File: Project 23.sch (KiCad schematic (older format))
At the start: 48 parts, among them J11 SRX 1, J12 SRX 2, J13 SWD, J21 Batt, J61 USB_Micro, Q51 Si2315, SW11 UI_Btn, SW12 SW_SPST, U1 STM32F103C(8-B)Tx, U2 MCP73811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

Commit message: Version 0.5
Removed 32k osc and added monting holes.
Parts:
- removed C13, C14: 20p, Capacitors_SMD:C_0805_HandSoldering, symbol Device:C
- removed Y12: 32khz, Project 23:ABS25, symbol Device:Crystal
- added M1, M2: Hole_M2, MountingHole:MountingHole_2.2mm_M2, symbol Connector_Generic:Conn_01x01
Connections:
- wire segments 287 -> 276
- no-connect marks 19 -> 23
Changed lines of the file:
@@
 $EndDescr
-$Comp
-L stm32:STM32F103C(8-B)Tx U1
-U 1 1 5B01BC59
-P 4550 2850
-F 0 "U1" H 4550 2950 50  0000 C CNN
-F 1 "STM32F103C(8-B)Tx" H 4550 2750 50  0000 C CNN
-F 2 "Housings_QFP:LQFP-48_7x7mm_Pitch0.5mm" H 4550 2650 50  0001 C CIN
-F 3 "" H 4550 2850 50  0000 C CNN
-	1    4550 2850
-	1    0    0    -1
-$EndComp
 $Comp
 L power:GND #PWR01
@@
 	1    0    0    -1
 $EndComp
-$Comp
-L Device:Crystal Y12
-U 1 1 5B055736
-P 900 2750
-F 0 "Y12" H 900 2900 50  0000 C CNN
-F 1 "32khz" H 900 2600 50  0000 C CNN
-F 2 "Project 23:ABS25" H 900 2750 50  0001 C CNN
-F 3 "" H 900 2750 50  0001 C CNN
-	1    900  2750
-	1    0    0    -1
-$EndComp
-$Comp
-L Device:C C14
-U 1 1 5B0560D6
-P 1050 3100
-F 0 "C14" H 1075 3200 50  0000 L CNN
-F 1 "20p" H 1075 3000 50  0000 L CNN
-F 2 "Capacitors_SMD:C_0805_HandSoldering" H 1088 2950 50  0001 C CNN
-F 3 "" H 1050 3100 50  0001 C CNN
-	1    1050 3100
-	1    0    0    -1
-$EndComp
-$Comp
-L Device:C C13
-U 1 1 5B0561ED
-P 750 3100
-F 0 "C13" H 775 3200 50  0000 L CNN
-F 1 "20p" H 775 3000 50  0000 L CNN
-F 2 "Capacitors_SMD:C_0805_HandSoldering" H 788 2950 50  0001 C CNN
-F 3 "" H 750 3100 50  0001 C CNN
-	1    750  3100
-	1    0    0    -1
-$EndComp
-$Comp
-L power:GND #PWR023
-U 1 1 5B05692F
-P 900 3400
-F 0 "#PWR023" H 900 3150 50  0001 C CNN
-F 1 "GND" H 900 3250 50  0000 C CNN
-F 2 "" H 900 3400 50  0001 C CNN
-F 3 "" H 900 3400 50  0001 C CNN
-	1    900  3400
-	1    0    0    -1
-$EndComp
 Text Label 8100 750  0    60   ~ 0
 Boost_En
@@
 Connection ~ 6050 6650
 Wire Wire Line
-	1050 2650 1150 2650
-Wire Wire Line
-	1050 2650 1050 2750
-Wire Wire Line
-	750  2550 750  2750
-Wire Wire Line
-	750  2550 1150 2550
-Connection ~ 750  2750
-Connection ~ 1050 2750
-Wire Wire Line
-	750  3250 750  3300
-Wire Wire Line
-	750  3300 900  3300
-Wire Wire Line
-	1050 3300 1050 3250
-Wire Wire Line
-	900  3400 900  3300
-Connection ~ 900  3300
-Wire Wire Line
 	9600 4250 10200 4250
 Wire Wire Line
@@
 	6050 6650 6050 6900
 Wire Wire Line
-	750  2750 750  2950
-Wire Wire Line
-	1050 2750 1050 2950
-Wire Wire Line
-	900  3300 1050 3300
-Wire Wire Line
 	10850 6200 10950 6200
 Wire Wire Line
@@
 Wire Wire Line
 	6300 5900 6600 5900
+$Comp
+L stm32:STM32F103C(8-B)Tx U1
+U 1 1 5B01BC59
+P 4550 2850
+F 0 "U1" H 4550 2950 50  0000 C CNN
+F 1 "STM32F103C(8-B)Tx" H 4550 2750 50  0000 C CNN
+F 2 "Housings_QFP:LQFP-48_7x7mm_Pitch0.5mm" H 4550 2650 50  0001 C CIN
+F 3 "" H 4550 2850 50  0000 C CNN
+	1    4550 2850
+	1    0    0    -1
+$EndComp
+NoConn ~ 1150 2550
+NoConn ~ 1150 2650
+$Comp
+L Connector_Generic:Conn_01x01 M1
+U 1 1 5BBF4E00
+P 6600 6350
+F 0 "M1" H 6679 6392 50  0000 L CNN
+F 1 "Hole_M2" H 6679 6301 50  0000 L CNN
+F 2 "MountingHole:MountingHole_2.2mm_M2" H 6600 6350 50  0001 C CNN
+F 3 "~" H 6600 6350 50  0001 C CNN
+	1    6600 6350
+	1    0    0    -1
+$EndComp
+$Comp
+L Connector_Generic:Conn_01x01 M2
+U 1 1 5BBF5814
+P 6600 6550
+F 0 "M2" H 6679 6592 50  0000 L CNN
+F 1 "Hole_M2" H 6679 6501 50  0000 L CNN
+F 2 "MountingHole:MountingHole_2.2mm_M2" H 6600 6550 50  0001 C CNN
+F 3 "~" H 6600 6550 50  0001 C CNN
+	1    6600 6550
+	1    0    0    -1
+$EndComp
+NoConn ~ 6400 6350
+NoConn ~ 6400 6550
 $EndSCHEMATC

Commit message: Reorganized sch
Move Sch over to a larger page, added physical drawing of borad.
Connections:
- wire segments 276 -> 273
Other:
- note added: "3V3 PSU\n"
- note added: "5V PSU\n"
- note added: "BATT CHR"
- note added: "ICSP\n\n"
- note added: "LED"
- note added: "OLED"
- note added: "SEN CON\n"
- note added: "UI BUTTONS\n"
- note added: "USB"
- moved on the sheet: C11, C12, C16, C17, C18, C19, C21, C22, C31, C32, C41, C42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

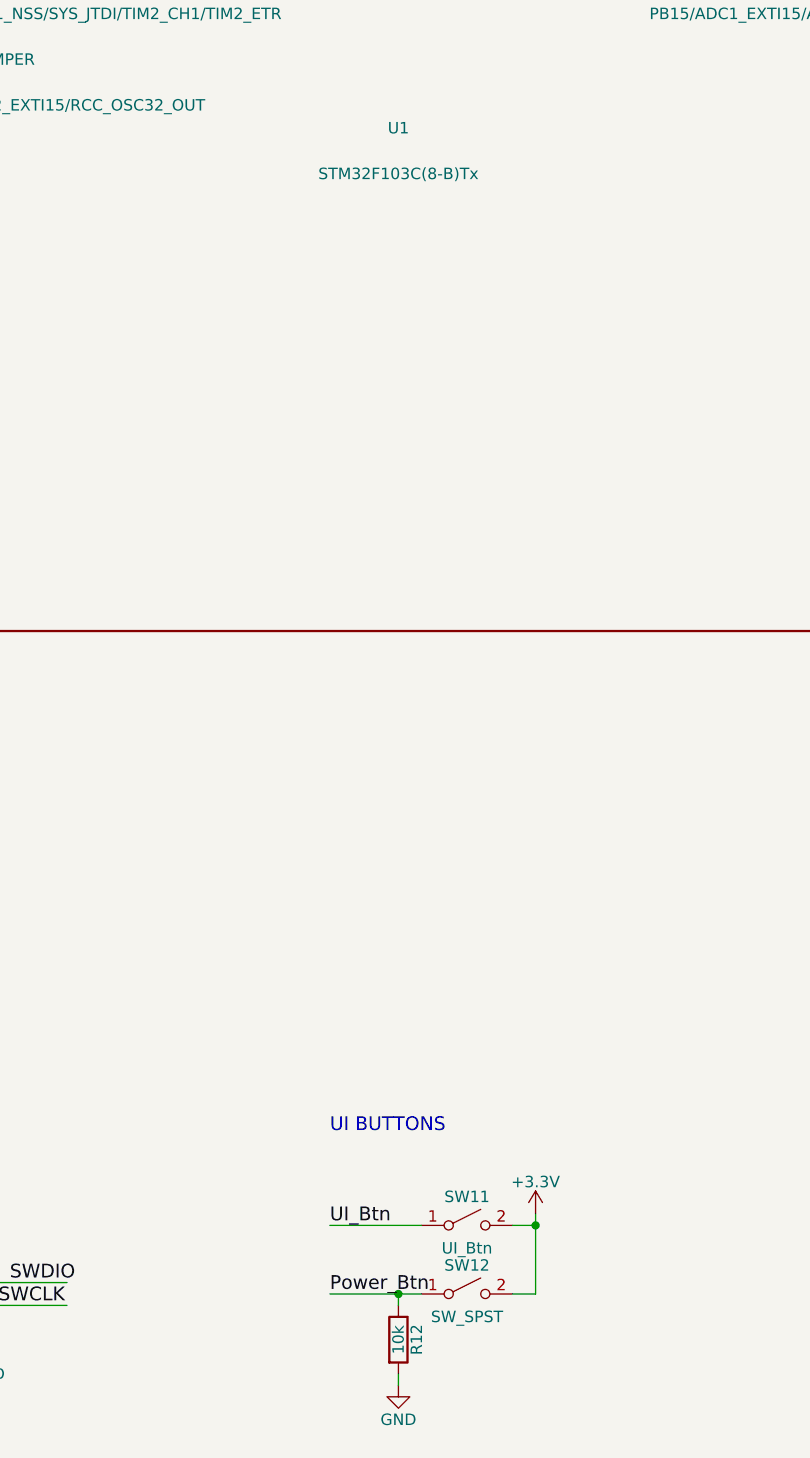
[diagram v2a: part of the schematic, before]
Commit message: Updated footprints to Kicad 5.0.0 librarys
Updated footprints to Kicad 5.0.0 Libraries. Switched C41 and C42 to EIA 3528-21 and EIA 6032-28 respectively.
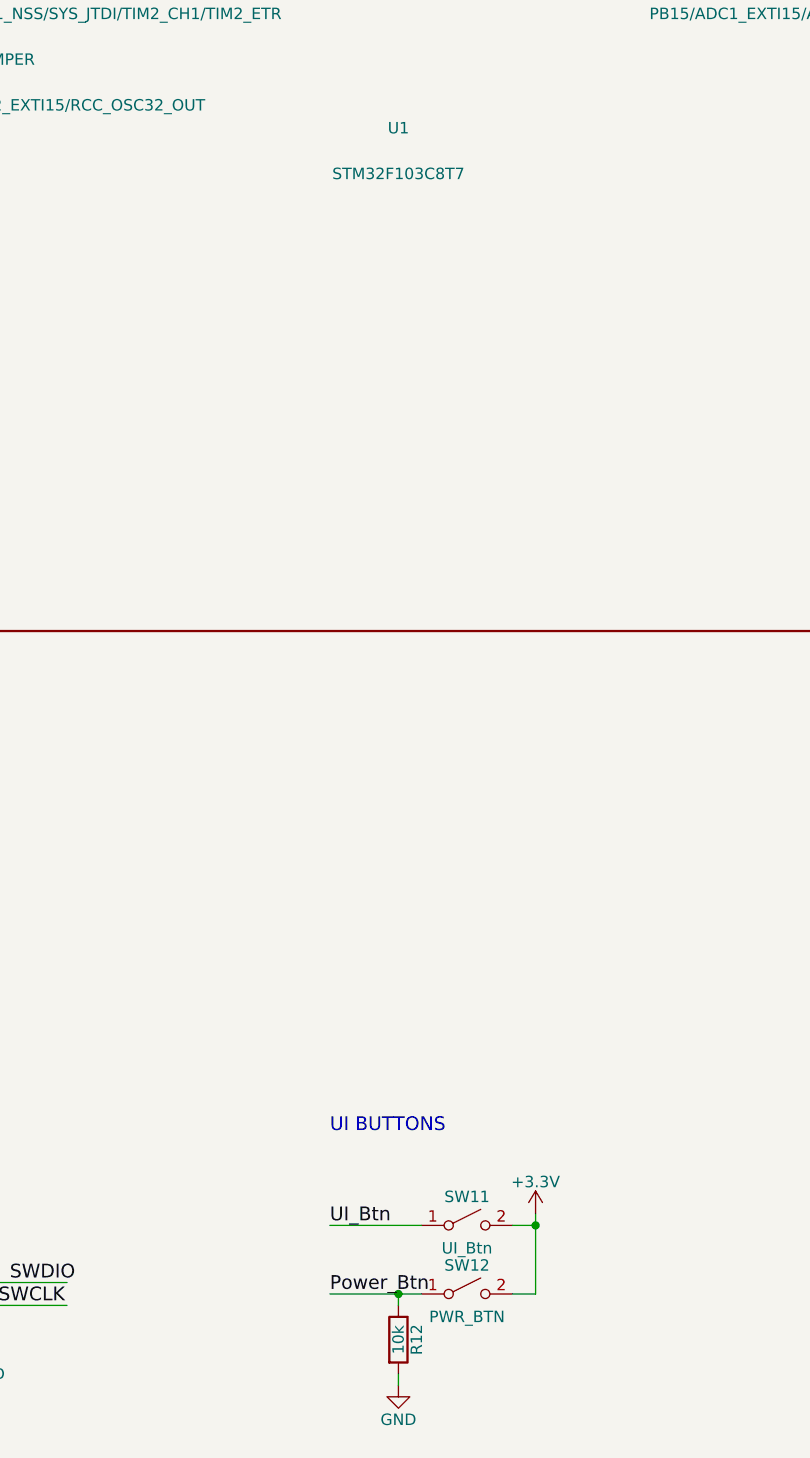
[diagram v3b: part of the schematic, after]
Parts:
- C11, C12, C16, C17, C18, C19, C21, C22, C31, C32: footprint Capacitors_SMD:C_0805_HandSoldering -> Capacitor_SMD:C_0805_2012Metric_Pad1.15x1.40mm_HandSolder
- C41: footprint Capacitors_Tantalum_SMD:CP_Tantalum_Case-A_EIA-3216-18_Hand -> Capacitor_Tantalum_SMD:CP_EIA-3528-21_Kemet-B_Pad1.50x2.35mm_HandSolder
- C42: footprint Capacitors_Tantalum_SMD:CP_Tantalum_Case-A_EIA-3216-18_Hand -> Capacitor_Tantalum_SMD:CP_EIA-6032-28_Kemet-C_Pad2.25x2.35mm_HandSolder
- D1, D2: footprint Diodes_SMD:D_SMB_Handsoldering -> Diode_SMD:D_SMB_Handsoldering
- D3, D4, D5: footprint LEDs:LED_0805_HandSoldering -> LED_SMD:LED_0805_2012Metric_Pad1.15x1.40mm_HandSolder
- D41: footprint Diodes_SMD:D_SMA_Handsoldering -> Diode_SMD:D_SMA_Handsoldering
- F11, F12: footprint Resistors_SMD:R_1206_HandSoldering -> Fuse:Fuse_1206_3216Metric_Pad1.42x1.75mm_HandSolder
- J11, J12: footprint Pin_Headers:Pin_Header_Angled_2x05_Pitch1.27mm -> Connector_PinHeader_1.27mm:PinHeader_2x05_P1.27mm_Horizontal
- J13: footprint Pin_Headers:Pin_Header_Angled_1x04_Pitch2.54mm -> Connector_PinHeader_2.54mm:PinHeader_1x04_P2.54mm_Horizontal
- J21: footprint Pin_Headers:Pin_Header_Straight_1x02_Pitch2.54mm -> Connector_PinHeader_2.54mm:PinHeader_1x02_P2.54mm_Vertical
- L41: footprint Resistors_SMD:R_1210_HandSoldering -> Inductor_SMD:L_1210_3225Metric_Pad1.42x2.65mm_HandSolder
- Q51: footprint TO_SOT_Packages_SMD:SOT-23_Handsoldering -> Package_TO_SOT_SMD:SOT-23_Handsoldering
- R12, R41, R51, R61, R62, R63, R64: footprint Resistors_SMD:R_0805_HandSoldering -> Resistor_SMD:R_0805_2012Metric_Pad1.15x1.40mm_HandSolder
- RN1, RN11, RN12: footprint Resistors_SMD:R_Array_Convex_4x0603 -> Resistor_SMD:R_Array_Convex_4x0603
- SW11: footprint Buttons_Switches_ThroughHole:SW_PUSH_6mm -> Button_Switch_THT:SW_PUSH_6mm_H5mm
- SW12: value SW_SPST -> PWR_BTN; footprint Buttons_Switches_ThroughHole:SW_PUSH_6mm -> Button_Switch_THT:SW_PUSH_6mm_H5mm
- U1: value STM32F103C(8-B)Tx -> STM32F103C8T7; footprint Housings_QFP:LQFP-48_7x7mm_Pitch0.5mm -> Package_QFP:LQFP-48_7x7mm_P0.5mm
- U2, U3, U4: footprint TO_SOT_Packages_SMD:SOT-23-5_HandSoldering -> Package_TO_SOT_SMD:SOT-23-5_HandSoldering
- U5: footprint Pin_Headers:Pin_Header_Straight_1x07_Pitch2.54mm -> Connector_PinSocket_2.54mm:PinSocket_1x07_P2.54mm_Vertical
- Y11: footprint Crystals:Crystal_HC49-U_Vertical -> Crystal:Crystal_HC49-4H_Vertical

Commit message: 0.7 Schmatic Design
Added SD card for logging,  Updated 3.3V power supplies to accont for addational power required by the sd card.  Added battery voltage messurment. Replaced battery charge IC with one that has a charge status output.
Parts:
- removed J21: Batt, Connector_PinHeader_2.54mm:PinHeader_1x02_P2.54mm_Vertical, symbol Project-23-rescue:Conn_01x02
- removed M1, M2: Hole_M2, MountingHole:MountingHole_2.2mm_M2, symbol Connector_Generic:Conn_01x01
- removed Q51: Si2315, Package_TO_SOT_SMD:SOT-23_Handsoldering, symbol Device:Q_PMOS_GSD
- removed R51: 10k, Resistor_SMD:R_0805_2012Metric_Pad1.15x1.40mm_HandSolder, symbol Device:R
- removed U2: MCP73811, Package_TO_SOT_SMD:SOT-23-5_HandSoldering, symbol Project-23-rescue:MCP73811_2
- added C33, C34: 1uF, Capacitor_SMD:C_0805_2012Metric_Pad1.15x1.40mm_HandSolder, symbol Device:C
- added C71: 1uF, symbol Device:C
- added D11: MMBD1205, symbol Device:D_x2_ACom_KKA
- added J21: BATT +, symbol Connector:Conn_01x01_Male
- added J71: Micro_SD_Card_Det, symbol Connector:Micro_SD_Card_Det
- added J?: BATT-, symbol Connector:Conn_01x01_Male
- added R11, R12, R21, R22, R81, R82, R83, R84: 10k, symbol Device:R
- added U21: MCP73832, symbol Project23-extras:MCP73832
- added U32: MIC5504, Package_TO_SOT_SMD:SOT-23-5_HandSoldering, symbol Project23-extras:NCP551
- C21: footprint Capacitor_SMD:C_0805_2012Metric_Pad1.15x1.40mm_HandSolder -> (none)
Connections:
- net labels added: 3V3SB, BATT_Mon, Batt_Mon, MISO2, MOSI2, PWR_EN, PWR_En, RXD, R_DIV_En, SCK2, SD_CD, SS2, TXD, Trigger, VBus_Mon
- net labels removed: Boost_En, OLED_En, USB_PU
- wire segments 273 -> 316
- no-connect marks 23 -> 15
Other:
- moved on the sheet: C11, C12, C22, C31, C32, J13, U1, U3, Y11

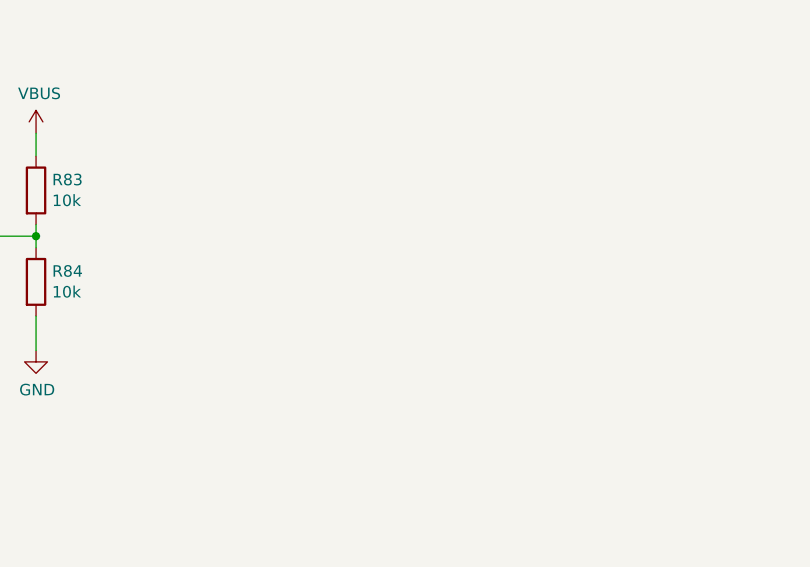
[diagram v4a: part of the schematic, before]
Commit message: Added Serial connector
added serial connector
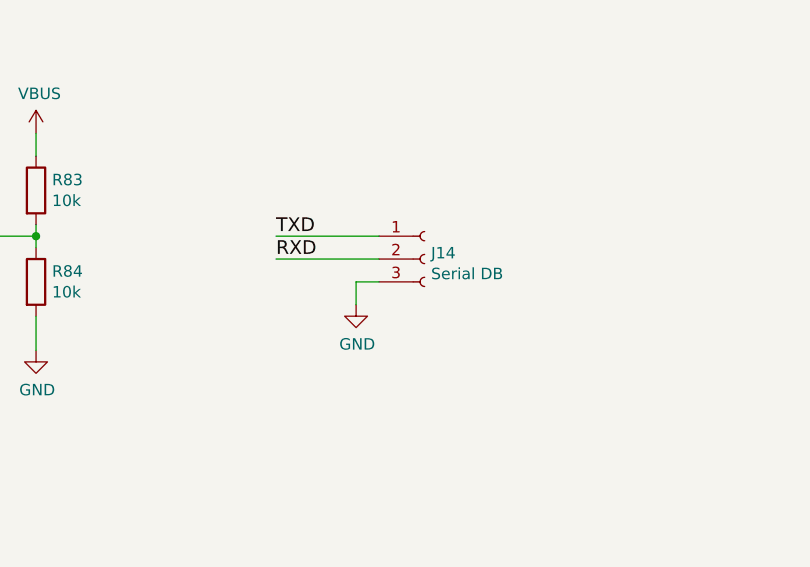
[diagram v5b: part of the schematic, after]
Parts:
- added J14: Serial DB, symbol Connector:Conn_01x03_Female
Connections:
- wire segments 316 -> 320
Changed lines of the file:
@@
+	1    0    0    -1
+$EndComp
+$Comp
+L Connector:Conn_01x03_Female J14
+U 1 1 5C591197
+P 7900 7500
+F 0 "J14" H 7928 7526 50  0000 L CNN
+F 1 "Serial DB" H 7928 7435 50  0000 L CNN
+F 2 "" H 7900 7500 50  0001 C CNN
+F 3 "~" H 7900 7500 50  0001 C CNN
+	1    7900 7500
+	1    0    0    -1
+$EndComp
+Wire Wire Line
+	7700 7400 7250 7400
+Wire Wire Line
+	7700 7500 7250 7500
+Wire Wire Line
+	7700 7600 7600 7600
+Wire Wire Line
+	7600 7600 7600 7700
+Text Label 7250 7400 0    60   ~ 0
+TXD
+Text Label 7250 7500 0    60   ~ 0
+RXD
+$Comp
+L power:GND #PWR?
+U 1 1 5C5E33AB
+P 7600 7700
+F 0 "#PWR?" H 7600 7450 50  0001 C CNN
+F 1 "GND" H 7605 7527 50  0000 C CNN
+F 2 "" H 7600 7700 50  0001 C CNN
+F 3 "" H 7600 7700 50  0001 C CNN
+	1    7600 7700
 	1    0    0    -1
 $EndComp
